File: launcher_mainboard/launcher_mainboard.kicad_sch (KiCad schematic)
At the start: 80 parts, among them J10 header, J11 header, J12 USB_C_Receptacle_USB2.0_16P, J2 Conn_01x06, J3 Conn_01x06, J4 Conn_01x06, J5 Conn_01x06, J6 bat_con, J7 fan_con, J8 ESC_1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

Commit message: more layout
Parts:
- removed Q2, Q3: MMBT3904, Package_TO_SOT_SMD:SOT-23, symbol Transistor_BJT:MMBT3904
- removed R11, R13: 10k, Resistor_SMD:R_0805_2012Metric, symbol Device:R
- removed U7: R-78E3.3-0.5, Converter_DCDC:Converter_DCDC_RECOM_R-78E-0.5_THT, symbol Regulator_Switching:R-78E3.3-0.5
- added U1: R-78E3.3-1.0, Converter_DCDC:Converter_DCDC_RECOM_R-78E-0.5_THT, symbol Regulator_Switching:R-78E3.3-1.0
- D1, D4, D5: footprint LED_SMD:LED_PLCC-2_3x2mm_AK -> LED_SMD:LED_0805_2012Metric
- D2: footprint Diode_SMD:D_0201_0603Metric -> Diode_SMD:D_0805_2012Metric
- D6: footprint Diode_THT:D_DO-35_SOD27_P5.08mm_Vertical_KathodeUp -> Diode_SMD:D_0805_2012Metric
- J7: footprint Connector_Molex:Molex_PicoBlade_53047-0210_1x02_P1.25mm_Vertical -> Connector_JST:JST_XH_B2B-XH-A_1x02_P2.50mm_Vertical
- Q1: value 2N7002H -> PJC7400; footprint Package_TO_SOT_SMD:SOT-23 -> Package_TO_SOT_SMD:SOT-323_SC-70
- R9: value 1.5k -> 680
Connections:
- net +3.3V: now also R3.2; no longer R10.1, R12.1
- net +3.3VBatt: now also U1.3 (OUT)
- net +BATT: now also U1.1 (IN)
- net -BATT: now also D4.1 (K), D5.1 (K), U1.2 (GND)
- net 3.3VUSB: no longer R3.2
- net ind_LED_1: now also R10.1
- net ind_LED_2: now also R12.1
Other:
- moved on the sheet: C3, C4, D1, D4, D5, R10, R12, R3, U10

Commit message: more layout
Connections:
- net -BATT: no longer J12.S1 (SHIELD)
- no-connect marks 58 -> 59
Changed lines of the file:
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@@
-	)
-	(junction
-		(at 30.48 264.16)
-		(diameter 0)
-		(color 0 0 0 0)
 	)
 	(junction
@@
 	)
 	(no_connect
+		(at 26.67 262.89)
+	)
+	(no_connect
 		(at 93.98 266.7)
 	)
@@
 	(wire
 		(pts
-			(xy 26.67 264.16) (xy 30.48 264.16)
-		)
-		(stroke
-			(width 0)
-			(type default)
-		)
-	)
-	(wire
-		(pts
 			(xy 175.26 213.36) (xy 175.26 215.9)
 		)
@@
 		)
 		(stroke
-			(width 0)
-			(type default)
-		)
-	)
-	(wire
-		(pts
-			(xy 26.67 262.89) (xy 26.67 264.16)
-		)
-		(stroke

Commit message: project restructure, switched out EDC IC, more layout
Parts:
- removed SW1: POWER_SWITCH, Button_Switch_SMD:SW_DIP_SPSTx01_Slide_9.78x4.72mm_W8.61mm_P2.54mm, symbol Switch:SW_DIP_x01
- removed U8: D3V3XA4B10LP, Package_DFN_QFN:Diodes_UDFN-10_1.0x2.5mm_P0.5mm, symbol Power_Protection:D3V3XA4B10LP
- added D3: DT1042-04SO-7, DT1042:SOT95P285X140-6N, symbol DT1042:DT1042-04SO-7
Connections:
- net +5VUSB: now also D3.5
- net -BATT: now also D3.2
- net USB_D+: now also D3.1
- net USB_D-: now also D3.3
- net at J6.2 (Pin_2): now also F1.1
- no-connect marks 59 -> 56
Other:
- moved on the sheet: J6

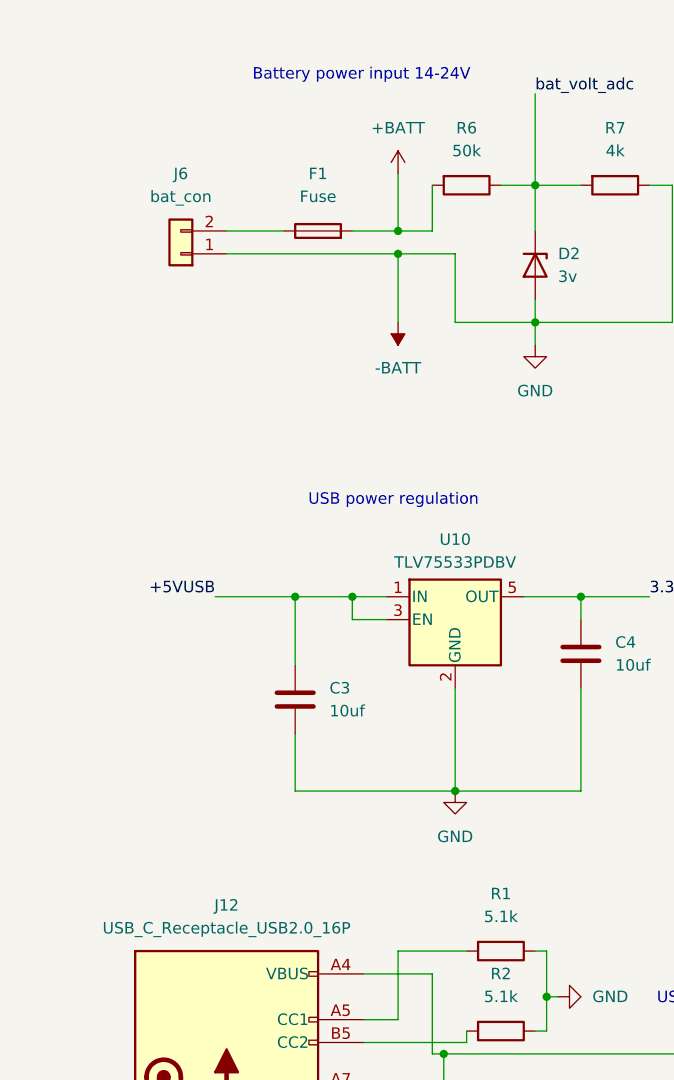
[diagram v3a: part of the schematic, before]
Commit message: renamed folder. How do differential pairs work?
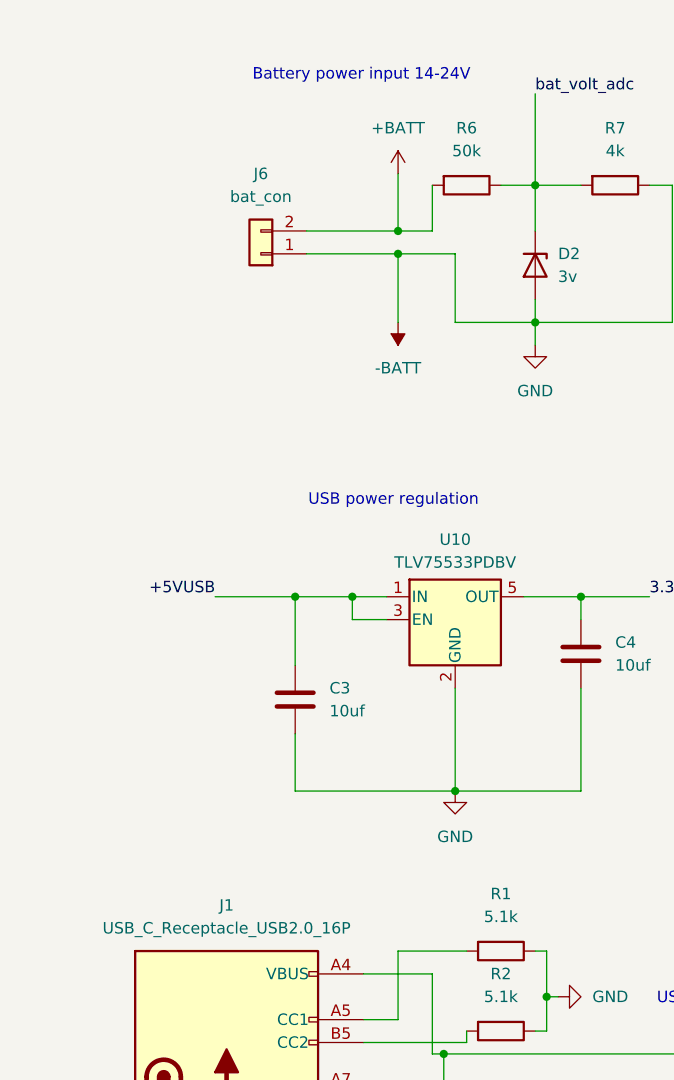
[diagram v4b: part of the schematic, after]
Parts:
- removed F1: Fuse, Fuse:Fuseholder_Clip-5x20mm_Bel_FC-203-22_Lateral_P17.80x5.00mm_D1.17mm_Horizontal, symbol Device:Fuse
- removed J12: USB_C_Receptacle_USB2.0_16P, Connector_USB:USB_C_Receptacle_JAE_DX07S016JA1R1500, symbol Connector:USB_C_Receptacle_USB2.0_16P
- added J1: USB_C_Receptacle_USB2.0_16P, Connector_USB:USB_C_Receptacle_GCT_USB4085, symbol Connector:USB_C_Receptacle_USB2.0_16P
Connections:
- net +5VUSB: now also J1.A4 (VBUS), J1.A9 (VBUS), J1.B4 (VBUS), J1.B9 (VBUS)
- net +BATT: now also J6.2 (Pin_2)
- net -BATT: now also J1.A1 (GND), J1.A12 (GND), J1.B1 (GND), J1.B12 (GND)
- net USB_D+: now also J1.A6 (D+), J1.B6 (D+)
- net USB_D-: now also J1.A7 (D-), J1.B7 (D-)
- net at R2.2: now also J1.B5 (CC2)
- net at R1.2: now also J1.A5 (CC1)
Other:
- moved on the sheet: J6
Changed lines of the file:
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@@
 	(wire
 		(pts
-			(xy 34.29 142.24) (xy 40.64 142.24)
+			(xy 43.18 142.24) (xy 53.34 142.24)
 		)
 		(stroke
@@
 	(wire
 		(pts
-			(xy 34.29 144.78) (xy 53.34 144.78)
+			(xy 43.18 144.78) (xy 53.34 144.78)
 		)
 		(stroke
@@
 	(wire
 		(pts
-			(xy 48.26 142.24) (xy 53.34 142.24)
-		)
-		(stroke
-			(width 0)
-			(type default)
-		)
-	)
-	(wire
-		(pts
 			(xy 53.34 92.71) (xy 53.34 54.61)
 		)
@@
 	(symbol
 		(lib_id "Connector_Generic:Conn_01x02")
-		(at 29.21 144.78 180)
+		(at 38.1 144.78 180)
 		(unit 1)
 		(exclude_from_sim no)
@@
 		(fields_autoplaced yes)
 		(property "Reference" "J6"
-			(at 29.21 135.89 0)
+			(at 38.1 135.89 0)
 			(effects
 				(font
@@
 		)
 		(property "Value" "bat_con"
-			(at 29.21 138.43 0)
+			(at 38.1 138.43 0)
 			(effects
 				(font
@@
 		)
 		(property "Footprint" "Connector_AMASS:AMASS_XT60-M_1x02_P7.20mm_Vertical"
-			(at 29.21 144.78 0)
+			(at 38.1 144.78 0)
 			(effects
 				(font
@@
 		)
 		(property "Datasheet" "~"
-			(at 29.21 144.78 0)
+			(at 38.1 144.78 0)
 			(effects
 				(font
@@
 		)
 		(property "Description" "Generic connector, single row, 01x02, script generated (kicad-library-utils/schlib/autogen/connector/)"
-			(at 29.21 144.78 0)
+			(at 38.1 144.78 0)
 			(effects
 				(font
@@
 	)
 	(symbol
+		(lib_id "Connector:USB_C_Receptacle_USB2.0_16P")
+		(at 34.29 240.03 0)
+		(unit 1)
+		(exclude_from_sim no)
+		(in_bom yes)
+		(on_board yes)
+		(dnp no)
+		(fields_autoplaced yes)
+		(property "Reference" "J1"
+			(at 34.29 217.17 0)
+			(effects
+				(font
+					(size 1.27 1.27)
+				)
+			)
+		)
+		(property "Value" "USB_C_Receptacle_USB2.0_16P"
+			(at 34.29 219.71 0)
+			(effects
+				(font
+					(size 1.27 1.27)
+				)
+			)
+		)
+		(property "Footprint" "Connector_USB:USB_C_Receptacle_GCT_USB4085"
+			(at 38.1 240.03 0)
+			(effects
+				(font
+					(size 1.27 1.27)
+				)
+				(hide yes)
+			)
+		)
+		(property "Datasheet" "https://www.usb.org/sites/default/files/documents/usb_type-c.zip"
+			(at 38.1 240.03 0)
+			(effects
+				(font
+					(size 1.27 1.27)
+				)
+				(hide yes)
+			)
+		)
+		(property "Description" "USB 2.0-only 16P Type-C Receptacle connector"
+			(at 34.29 240.03 0)
+			(effects
+				(font
+					(size 1.27 1.27)
+				)
+				(hide yes)
+			)
+		)
+		(pin "S1"
+		)
+		(pin "A6"
+		)
+		(pin "B1"
+		)
+		(pin "A5"
+		)
+		(pin "B4"
+		)
+		(pin "B6"
+		)
+		(pin "B9"
+		)
+		(pin "A7"
+		)
+		(pin "A8"
+		)
+		(pin "A1"
+		)
+		(pin "A12"
+		)
+		(pin "A4"
+		)
+		(pin "A9"
+		)
+		(pin "B7"
+		)
+		(pin "B5"
+		)
+		(pin "B8"
+		)
+		(pin "B12"
+		)
+		(instances
+			(project "launcher_mainboard"
+				(path "/c708c50f-809b-4d12-a774-1744101f70a6"
+					(reference "J1")
+					(unit 1)
+				)
+			)
+		)
+	)
+	(symbol
 		(lib_id "Connector_Generic:Conn_01x02")
 		(at 161.29 26.67 0)
@@
 	)
 	(symbol
-		(lib_id "Connector:USB_C_Receptacle_USB2.0_16P")
-		(at 34.29 240.03 0)
-		(unit 1)
-		(exclude_from_sim no)
-		(in_bom yes)
-		(on_board yes)
-		(dnp no)
-		(fields_autoplaced yes)
-		(property "Reference" "J12"
-			(at 34.29 217.17 0)
-			(effects
-				(font
-					(size 1.27 1.27)
-				)
-			)
-		)
-		(property "Value" "USB_C_Receptacle_USB2.0_16P"
-			(at 34.29 219.71 0)
-			(effects
-				(font
-					(size 1.27 1.27)
-				)
-			)
-		)
-		(property "Footprint" "Connector_USB:USB_C_Receptacle_JAE_DX07S016JA1R1500"
-			(at 38.1 240.03 0)
-			(effects
-				(font
-					(size 1.27 1.27)
-				)
-				(hide yes)
-			)
-		)
-		(property "Datasheet" "https://www.usb.org/sites/default/files/documents/usb_type-c.zip"
-			(at 38.1 240.03 0)
-			(effects
-				(font
-					(size 1.27 1.27)
-				)
-				(hide yes)
-			)
-		)
-		(property "Description" "USB 2.0-only 16P Type-C Receptacle connector"
-			(at 34.29 240.03 0)
-			(effects
-				(font
-					(size 1.27 1.27)
-				)
-				(hide yes)
-			)
-		)
-		(pin "S1"
-		)
-		(pin "B6"
-		)
-		(pin "B5"
-		)
-		(pin "B12"
-		)
-		(pin "A5"
-		)
-		(pin "A7"
-		)
-		(pin "A12"
-		)
-		(pin "A8"
-		)
-		(pin "B4"
-		)
-		(pin "B8"
-		)
-		(pin "B9"
-		)
-		(pin "B7"
-		)
-		(pin "A4"
-		)
-		(pin "A6"
-		)
-		(pin "B1"
-		)
-		(pin "A1"
-		)
-		(pin "A9"
-		)
-		(instances
-			(project "launcher_mainboard"
-				(path "/c708c50f-809b-4d12-a774-1744101f70a6"
-					(reference "J12")
-					(unit 1)
-				)
-			)
-		)
-	)
-	(symbol
 		(lib_id "Device:R")
 		(at 196.85 259.08 180)
@@
 					(unit 1)
 				)
-			)
-		)
-	)
-	(symbol
-		(lib_id "Device:Fuse")
-		(at 44.45 142.24 90)
-		(unit 1)
-		(exclude_from_sim no)
-		(in_bom yes)
-		(on_board yes)
-		(dnp no)
-		(fields_autoplaced yes)
-		(property "Reference" "F1"
-			(at 44.45 135.89 90)
-			(effects
-				(font
-					(size 1.27 1.27)
-				)
-			)
-		)
-		(property "Value" "Fuse"
-			(at 44.45 138.43 90)
-			(effects
-				(font
-					(size 1.27 1.27)
-				)
-			)
-		)
-		(property "Footprint" "Fuse:Fuseholder_Clip-5x20mm_Bel_FC-203-22_Lateral_P17.80x5.00mm_D1.17mm_Horizontal"
-			(at 44.45 144.018 90)
-			(effects
-				(font
-					(size 1.27 1.27)
-				)
-				(hide yes)
-			)
-		)
-		(property "Datasheet" "~"
-			(at 44.45 142.24 0)
-			(effects
-				(font
-					(size 1.27 1.27)
-				)
-				(hide yes)
-			)
-		)
-		(property "Description" "Fuse"
-			(at 44.45 142.24 0)
-			(effects
-				(font
-					(size 1.27 1.27)
-				)
-				(hide yes)
-			)
-		)
-		(pin "1"
-		)
-		(pin "2"
-		)
-		(instances
-			(project "launcher_mainboard"
-				(path "/c708c50f-809b-4d12-a774-1744101f70a6"
-					(reference "F1")
-					(unit 1)
-				)

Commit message: pre usb change
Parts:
- added C14, C17, C18, C6: 10uf, Capacitor_SMD:C_0805_2012Metric, symbol Device:C
- added H1, H2, H3, H4: MountingHole, MountingHole:MountingHole_3.2mm_M3_Pad_TopBottom, symbol Mechanical:MountingHole
- U6: footprint RF_Module:ESP32-S3-WROOM-1 -> CustomFootprints:ESP32-S3-WROOM-1
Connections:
- net +BATT: now also C14.1, C17.2, C18.2, C6.1
- net -BATT: now also C14.2, C17.1, C18.1, C6.2
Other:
- moved on the sheet: C10, C11, C12, C9

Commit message: switched to SMD USB C connector
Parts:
- J1: footprint Connector_USB:USB_C_Receptacle_GCT_USB4085 -> Connector_USB:USB_C_Receptacle_GCT_USB4105-xx-A_16P_TopMnt_Horizontal
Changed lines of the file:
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@@
 			)
 		)
-		(property "Footprint" "Connector_USB:USB_C_Receptacle_GCT_USB4085"
+		(property "Footprint" "Connector_USB:USB_C_Receptacle_GCT_USB4105-xx-A_16P_TopMnt_Horizontal"
 			(at 38.1 240.03 0)
 			(effects

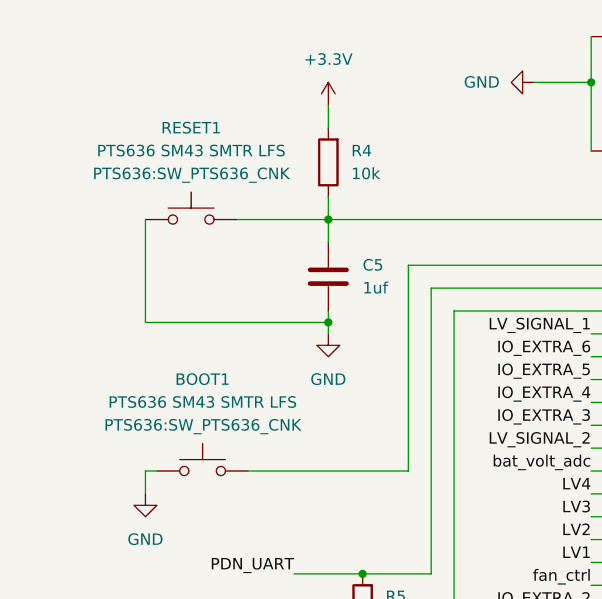
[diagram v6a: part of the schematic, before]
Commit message: design rule fixes
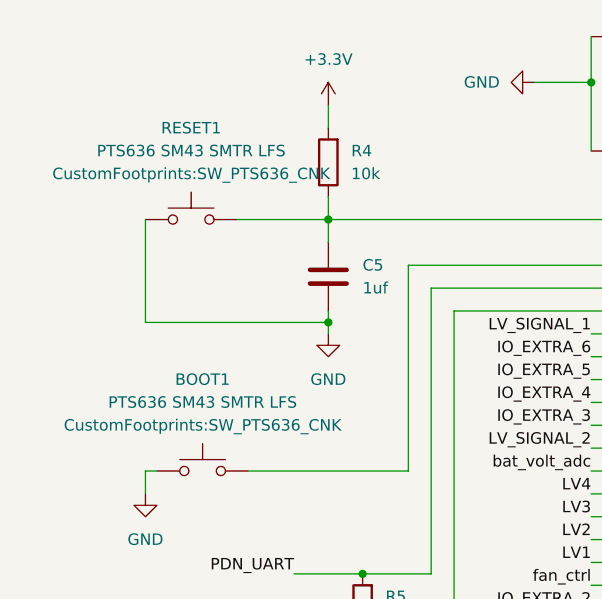
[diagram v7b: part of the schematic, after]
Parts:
- BOOT1, RESET1: footprint PTS636:SW_PTS636_CNK -> CustomFootprints:SW_PTS636_CNK
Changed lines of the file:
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@@
 			)
 		)
-		(property "Footprint" "PTS636:SW_PTS636_CNK"
+		(property "Footprint" "CustomFootprints:SW_PTS636_CNK"
 			(at 24.13 39.37 0)
 			(effects
@@
 			)
 		)
-		(property "Footprint" "PTS636:SW_PTS636_CNK"
+		(property "Footprint" "CustomFootprints:SW_PTS636_CNK"
 			(at 25.4 67.31 0)
 			(effects

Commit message: more layout
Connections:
- no-connect marks 56 -> 64
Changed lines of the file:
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@@
+	)
+	(no_connect
+		(at 386.08 160.02)
 	)
 	(no_connect
@@
 	)
 	(no_connect
+		(at 386.08 96.52)
+	)
+	(no_connect
 		(at 340.36 143.51)
 	)
 	(no_connect
 		(at 49.53 255.27)
+	)
+	(no_connect
+		(at 386.08 104.14)
 	)
 	(no_connect
@@
 	(no_connect
 		(at 340.36 57.15)
+	)
+	(no_connect
+		(at 386.08 152.4)
 	)
 	(no_connect
@@
 	)
 	(no_connect
+		(at 386.08 208.28)
+	)
+	(no_connect
 		(at 289.56 52.07)
 	)
@@
 	(no_connect
 		(at 289.56 212.09)
+	)
+	(no_connect
+		(at 386.08 39.37)
 	)
 	(no_connect
@@
 	)
 	(no_connect
+		(at 386.08 215.9)
+	)
+	(no_connect
 		(at 289.56 92.71)
 	)
@@
 	)
 	(no_connect
+		(at 386.08 46.99)
+	)
+	(no_connect
